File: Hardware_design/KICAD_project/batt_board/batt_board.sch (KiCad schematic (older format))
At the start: 52 parts, among them J11 battery_plug_in, J2 Conn_01x02, J3 Conn_01x02, J4 Conn_01x02, J5 Conn_01x02, U1 TPS5430DDA, U2 AMS1117-3.3

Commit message: batt board: refine the name of sockets
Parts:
- C3: footprint Capacitor_SMD:C_0603_1608Metric_Pad1.08x0.95mm_HandSolder -> Capacitor_Tantalum_SMD:CP_EIA-3528-21_Kemet-B
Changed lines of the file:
@@
 	8100 2700 8700 2700
-Wire Wire Line
-	8200 2800 8200 3050
 Wire Wire Line
 	8200 2800 8700 2800
@@
 $EndComp
 $Comp
-L Device:R_Small_US R11
-U 1 1 60410FC3
-P 8300 3150
-F 0 "R11" H 8368 3196 50  0000 L CNN
-F 1 "22" H 8368 3105 50  0000 L CNN
-F 2 "Resistor_SMD:R_0603_1608Metric_Pad0.98x0.95mm_HandSolder" H 8300 3150 50  0001 C CNN
-F 3 "~" H 8300 3150 50  0001 C CNN
-	1    8300 3150
-	1    0    0    -1
-$EndComp
-$Comp
-L Device:R_Small_US R12
-U 1 1 604142BD
-P 8400 3150
-F 0 "R12" H 8468 3196 50  0000 L CNN
-F 1 "22" H 8468 3105 50  0000 L CNN
-F 2 "Resistor_SMD:R_0603_1608Metric_Pad0.98x0.95mm_HandSolder" H 8400 3150 50  0001 C CNN
-F 3 "~" H 8400 3150 50  0001 C CNN
-	1    8400 3150
-	1    0    0    -1
-$EndComp
-$Comp
 L Device:R_Small_US R13
 U 1 1 60417C9B
@@
 	8200 3250 8200 3350
 Wire Wire Line
-	8300 3050 8300 2900
-Wire Wire Line
 	8400 3250 8400 3350
 Wire Wire Line
@@
 F 0 "C3" H 3191 2146 50  0000 L CNN
 F 1 "220uF" H 3191 2055 50  0000 L CNN
-F 2 "Capacitor_SMD:C_0603_1608Metric_Pad1.08x0.95mm_HandSolder" H 3100 2100 50  0001 C CNN
+F 2 "Capacitor_Tantalum_SMD:CP_EIA-3528-21_Kemet-B" H 3100 2100 50  0001 C CNN
 F 3 "~" H 3100 2100 50  0001 C CNN
 	1    3100 2100
@@
 	1650 2150 950  2150
 Connection ~ 1650 2150
+Wire Wire Line
+	8300 3050 8300 2900
+Wire Wire Line
+	8200 2800 8200 3050
+$Comp
+L Device:R_Small_US R11
+U 1 1 60410FC3
+P 8300 3150
+F 0 "R11" H 8368 3196 50  0000 L CNN
+F 1 "22" H 8368 3105 50  0000 L CNN
+F 2 "Resistor_SMD:R_0603_1608Metric_Pad0.98x0.95mm_HandSolder" H 8300 3150 50  0001 C CNN
+F 3 "~" H 8300 3150 50  0001 C CNN
+	1    8300 3150
+	1    0    0    -1
+$EndComp
+$Comp
+L Device:R_Small_US R12
+U 1 1 604142BD
+P 8400 3150
+F 0 "R12" H 8468 3196 50  0000 L CNN
+F 1 "22" H 8468 3105 50  0000 L CNN
+F 2 "Resistor_SMD:R_0603_1608Metric_Pad0.98x0.95mm_HandSolder" H 8400 3150 50  0001 C CNN
+F 3 "~" H 8400 3150 50  0001 C CNN
+	1    8400 3150
+	1    0    0    -1
+$EndComp
 $EndSCHEMATC

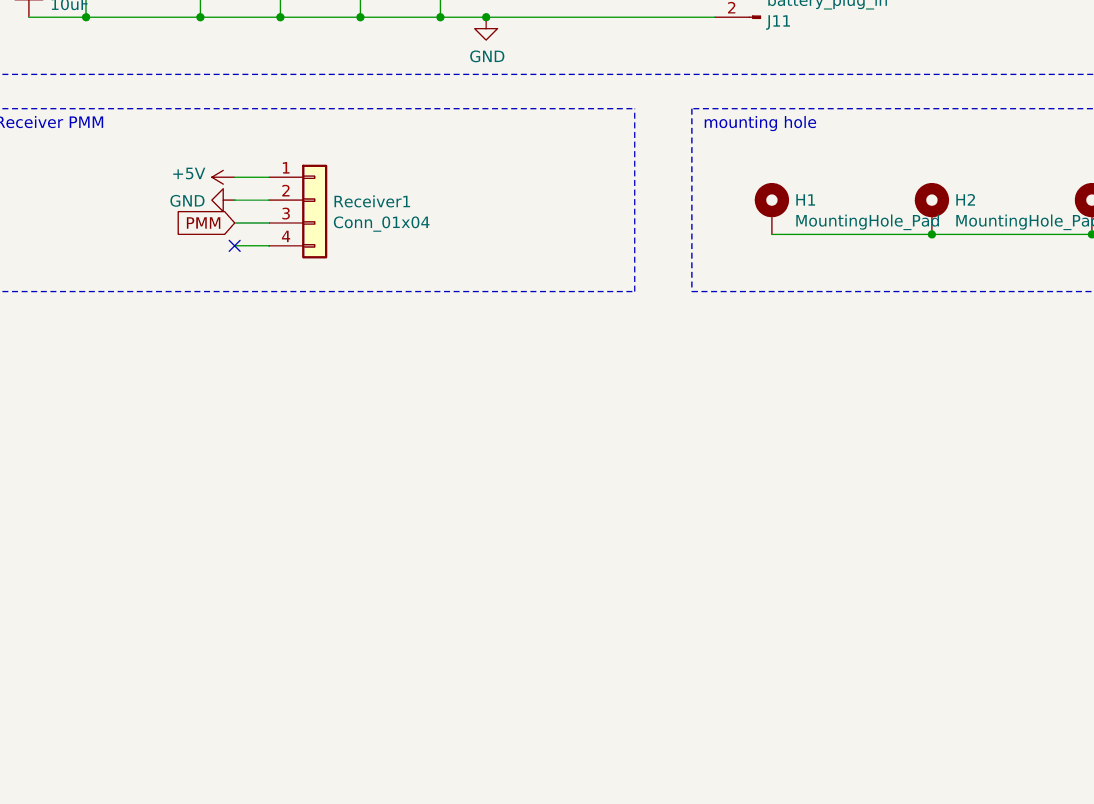
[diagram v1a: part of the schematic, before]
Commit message: 完善了供电板，增加了 IMU的外围传感电路设计
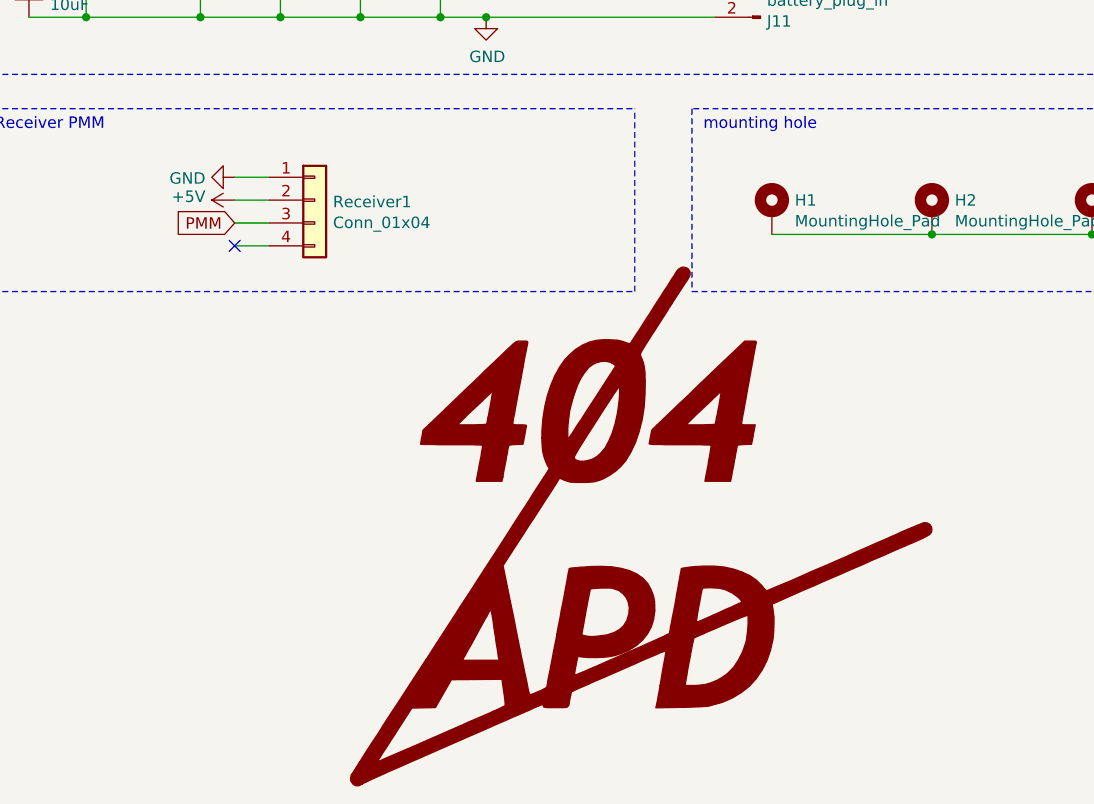
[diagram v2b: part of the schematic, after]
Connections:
- net +5V: now also Receiver1.2 (Pin_2); no longer Receiver1.1 (Pin_1)
- net GND: now also Receiver1.1 (Pin_1); no longer Receiver1.2 (Pin_2)
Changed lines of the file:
@@
 L power:GND #PWR0105
 U 1 1 602F3780
-P 1600 5100
-F 0 "#PWR0105" H 1600 4850 50  0001 C CNN
-F 1 "GND" V 1605 4972 50  0000 R CNN
-F 2 "" H 1600 5100 50  0001 C CNN
-F 3 "" H 1600 5100 50  0001 C CNN
-	1    1600 5100
+P 1600 5000
+F 0 "#PWR0105" H 1600 4750 50  0001 C CNN
+F 1 "GND" V 1605 4872 50  0000 R CNN
+F 2 "" H 1600 5000 50  0001 C CNN
+F 3 "" H 1600 5000 50  0001 C CNN
+	1    1600 5000
 	0    1    1    0
 $EndComp
@@
 L power:+5V #PWR0103
 U 1 1 604C3AB9
-P 1600 5000
-F 0 "#PWR0103" H 1600 4850 50  0001 C CNN
-F 1 "+5V" V 1615 5128 50  0000 L CNN
-F 2 "" H 1600 5000 50  0001 C CNN
-F 3 "" H 1600 5000 50  0001 C CNN
-	1    1600 5000
+P 1600 5100
+F 0 "#PWR0103" H 1600 4950 50  0001 C CNN
+F 1 "+5V" V 1615 5228 50  0000 L CNN
+F 2 "" H 1600 5100 50  0001 C CNN
+F 3 "" H 1600 5100 50  0001 C CNN
+	1    1600 5100
 	0    -1   -1   0
 $EndComp
@@
 	1    0    0    -1
 $EndComp
+$Comp
+L 404APD:LOGO #G1
+U 1 1 603449C8
+P 3350 6550
+F 0 "#G1" H 3350 5217 60  0001 C CNN
+F 1 "LOGO" H 3350 7883 60  0001 C CNN
+F 2 "" H 3350 6550 50  0001 C CNN
+F 3 "" H 3350 6550 50  0001 C CNN
+	1    3350 6550
+	1    0    0    -1
+$EndComp

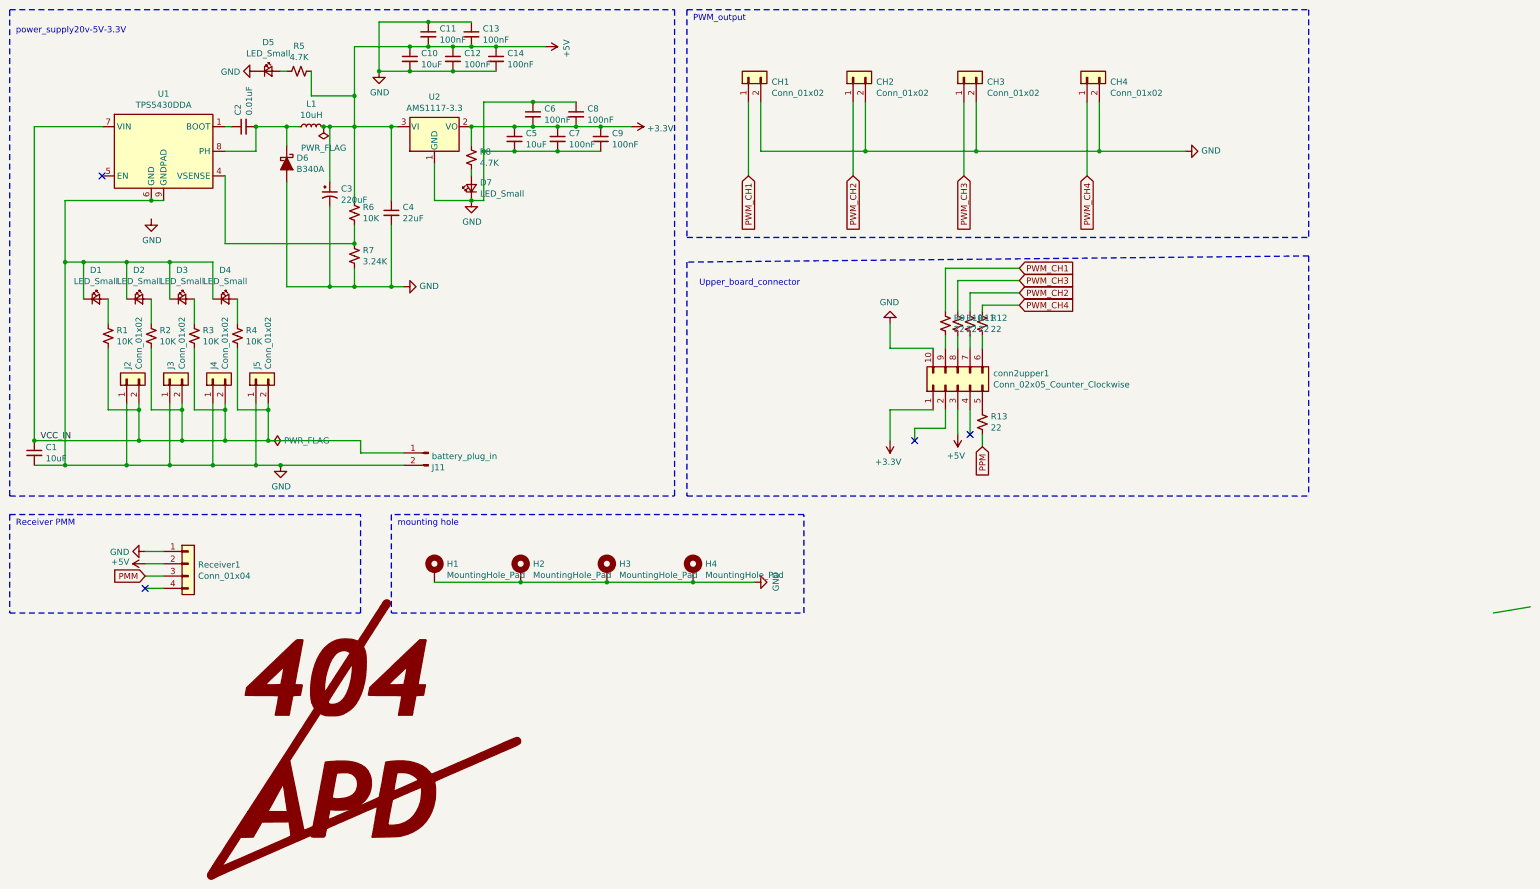
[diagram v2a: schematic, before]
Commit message: 控制系统硬件设计完成，电源板正式发布v1.0.0 控制板打样v0.2.0测试
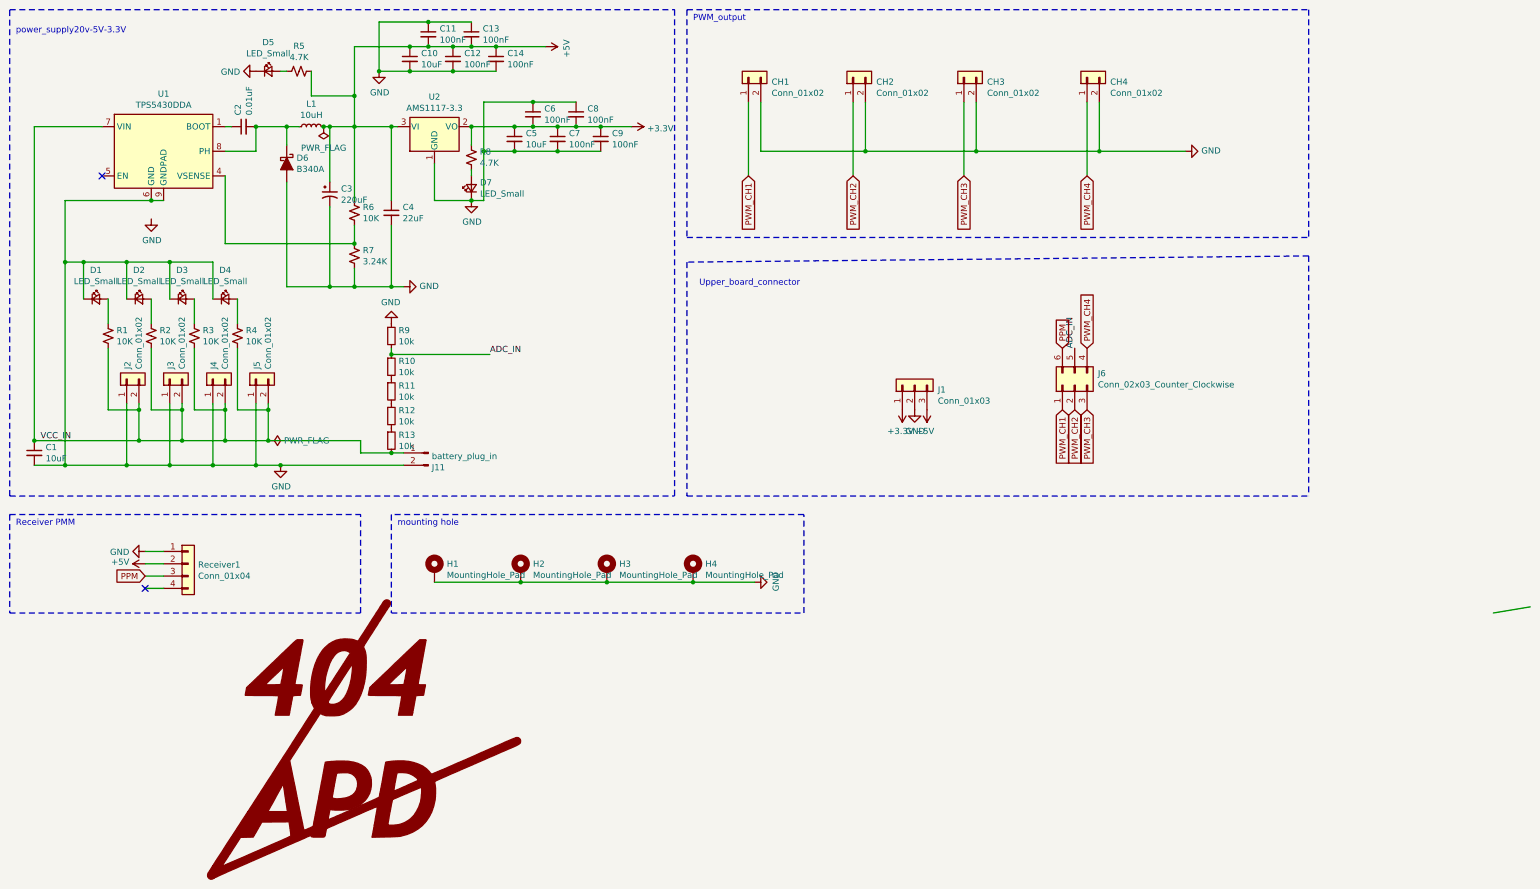
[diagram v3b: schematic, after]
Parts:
- removed R10, R11, R12, R13, R9: 22, Resistor_SMD:R_0603_1608Metric_Pad0.98x0.95mm_HandSolder, symbol Device:R_Small_US
- removed conn2upper1: Conn_02x05_Counter_Clockwise, Connector_PinSocket_2.54mm:PinSocket_2x05_P2.54mm_Horizontal, symbol Connector_Generic:Conn_02x05_Counter_Clockwise
- added J1: Conn_01x03, Connector_PinSocket_2.54mm:PinSocket_1x03_P2.54mm_Vertical, symbol Connector_Generic:Conn_01x03
- added J6: Conn_02x03_Counter_Clockwise, Connector_PinSocket_1.27mm:PinSocket_2x03_P1.27mm_Vertical_SMD, symbol Connector_Generic:Conn_02x03_Counter_Clockwise
- added R10, R11, R12, R13, R9: 10k, Resistor_SMD:R_0603_1608Metric_Pad0.98x0.95mm_HandSolder, symbol Device:R_Small
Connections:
- net PMM is gone; now on net PPM: Receiver1.3 (Pin_3)
- net +3V3: now also J1.1 (Pin_1)
- net +5V: now also J1.3 (Pin_3)
- net GND: now also J1.2 (Pin_2), R9.1
- net PPM: now also J6.6 (Pin_6)
- net PWM_CH1: now also J6.1 (Pin_1)
- net PWM_CH2: now also J6.2 (Pin_2)
- net PWM_CH3: now also J6.3 (Pin_3)
- net PWM_CH4: now also J6.4 (Pin_4)
- net VCC_IN: now also R13.2
- new net: R12.2, R13.1
- new net: R11.2, R12.1
- new net: R10.2, R11.1
- new net ADC_IN: J6.5 (Pin_5), R10.1, R9.2
- no-connect marks 4 -> 2
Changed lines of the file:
@@
 Sheet 1 1
 Title "power_suplly"
-Date "2021-02-14"
-Rev "0.1"
+Date "2021-03-01"
+Rev "0.2"
 Comp ""
 Comment1 ""
@@
 	1600 5100 1750 5100
 Text GLabel 1600 5200 0    50   Input ~ 0
-PMM
+PPM
 Wire Wire Line
 	1750 5300 1600 5300
@@
 Upper_board_connector\n
 $Comp
-L Connector_Generic:Conn_02x05_Counter_Clockwise conn2upper1
-U 1 1 603BA7D0
-P 8200 3650
-F 0 "conn2upper1" V 8296 3362 50  0000 R CNN
-F 1 "Conn_02x05_Counter_Clockwise" V 8205 3362 50  0000 R CNN
-F 2 "Connector_PinSocket_2.54mm:PinSocket_2x05_P2.54mm_Horizontal" H 8200 3650 50  0001 C CNN
-F 3 "~" H 8200 3650 50  0001 C CNN
-	1    8200 3650
-	0    -1   -1   0
-$EndComp
-Wire Wire Line
-	8000 3350 7650 3350
-Wire Wire Line
-	8000 3850 7650 3850
-Wire Wire Line
-	7650 3850 7650 4100
-$Comp
 L power:GND #PWR0109
 U 1 1 603C3758
-P 7650 3150
-F 0 "#PWR0109" H 7650 2900 50  0001 C CNN
-F 1 "GND" H 7655 2977 50  0000 C CNN
-F 2 "" H 7650 3150 50  0001 C CNN
-F 3 "" H 7650 3150 50  0001 C CNN
-	1    7650 3150
-	-1   0    0    1
-$EndComp
-Wire Wire Line
-	8200 3850 8200 4050
-Wire Wire Line
-	8300 3850 8300 4050
-Text GLabel 8700 2700 2    50   Input ~ 0
+P 7850 3850
+F 0 "#PWR0109" H 7850 3600 50  0001 C CNN
+F 1 "GND" H 7855 3677 50  0000 C CNN
+F 2 "" H 7850 3850 50  0001 C CNN
+F 3 "" H 7850 3850 50  0001 C CNN
+	1    7850 3850
+	1    0    0    -1
+$EndComp
+Text GLabel 9050 3850 3    50   Input ~ 0
 PWM_CH1
-Text GLabel 8700 2800 2    50   Input ~ 0
+Text GLabel 9250 3850 3    50   Input ~ 0
 PWM_CH3
-Text GLabel 8700 2900 2    50   Input ~ 0
+Text GLabel 9150 3850 3    50   Input ~ 0
 PWM_CH2
-Text GLabel 8700 3000 2    50   Input ~ 0
+Text GLabel 9250 3350 1    50   Input ~ 0
 PWM_CH4
-Text GLabel 8400 4150 3    50   Input ~ 0
+Text GLabel 9050 3350 1    50   Input ~ 0
 PPM
-NoConn ~ 8300 4050
-Wire Wire Line
-	8100 3350 8100 3250
-Wire Wire Line
-	8100 2700 8700 2700
-Wire Wire Line
-	8200 2800 8700 2800
-Wire Wire Line
-	8300 3350 8300 3250
-Wire Wire Line
-	8300 2900 8700 2900
-Wire Wire Line
-	8400 3000 8400 3050
-Wire Wire Line
-	8400 3000 8700 3000
-$Comp
-L Device:R_Small_US R9
-U 1 1 60408BAB
-P 8100 3150
-F 0 "R9" H 8168 3196 50  0000 L CNN
-F 1 "22" H 8168 3105 50  0000 L CNN
-F 2 "Resistor_SMD:R_0603_1608Metric_Pad0.98x0.95mm_HandSolder" H 8100 3150 50  0001 C CNN
-F 3 "~" H 8100 3150 50  0001 C CNN
-	1    8100 3150
-	1    0    0    -1
-$EndComp
-Wire Wire Line
-	8100 3050 8100 2700
-$Comp
-L Device:R_Small_US R10
-U 1 1 6040DAE6
-P 8200 3150
-F 0 "R10" H 8268 3196 50  0000 L CNN
-F 1 "22" H 8268 3105 50  0000 L CNN
-F 2 "Resistor_SMD:R_0603_1608Metric_Pad0.98x0.95mm_HandSolder" H 8200 3150 50  0001 C CNN
-F 3 "~" H 8200 3150 50  0001 C CNN
-	1    8200 3150
-	1    0    0    -1
-$EndComp
-$Comp
-L Device:R_Small_US R13
-U 1 1 60417C9B
-P 8400 3950
-F 0 "R13" H 8468 3996 50  0000 L CNN
-F 1 "22" H 8468 3905 50  0000 L CNN
-F 2 "Resistor_SMD:R_0603_1608Metric_Pad0.98x0.95mm_HandSolder" H 8400 3950 50  0001 C CNN
-F 3 "~" H 8400 3950 50  0001 C CNN
-	1    8400 3950
-	1    0    0    -1
-$EndComp
 $Comp
 L power:GND #PWR0111
@@
 	3100 2200 3100 2850
 Wire Wire Line
-	8200 3250 8200 3350
-Wire Wire Line
-	8400 3250 8400 3350
-Wire Wire Line
 	2500 1550 2750 1550
 Wire Wire Line
@@
 Wire Wire Line
 	3100 1550 3300 1550
-Wire Wire Line
-	8400 4050 8400 4150
 $Comp
 L power:+3.3V #PWR0110
 U 1 1 603C41F2
-P 7650 4100
-F 0 "#PWR0110" H 7650 3950 50  0001 C CNN
-F 1 "+3.3V" H 7665 4273 50  0000 C CNN
-F 2 "" H 7650 4100 50  0001 C CNN
-F 3 "" H 7650 4100 50  0001 C CNN
-	1    7650 4100
+P 7750 3850
+F 0 "#PWR0110" H 7750 3700 50  0001 C CNN
+F 1 "+3.3V" H 7765 4023 50  0000 C CNN
+F 2 "" H 7750 3850 50  0001 C CNN
+F 3 "" H 7750 3850 50  0001 C CNN
+	1    7750 3850
 	-1   0    0    1
 $EndComp
@@
 Wire Wire Line
 	5350 5250 6050 5250
-Wire Wire Line
-	6050 5250 6550 5250
 Connection ~ 6050 5250
-$Comp
-L power:GND #PWR0104
-U 1 1 60310458
-P 6550 5250
-F 0 "#PWR0104" H 6550 5000 50  0001 C CNN
-F 1 "GND" H 6555 5077 50  0000 C CNN
-F 2 "" H 6550 5250 50  0001 C CNN
-F 3 "" H 6550 5250 50  0001 C CNN
-	1    6550 5250
-	0    -1   -1   0
-$EndComp
 Connection ~ 950  4300
 Wire Wire Line
@@
 	3350 4100 3350 4200
 Wire Wire Line
-	3350 4200 3700 4200
+	3350 4200 3600 4200
 Wire Wire Line
 	1300 3850 1550 3850
@@
 Wire Wire Line
 	1750 5000 1600 5000
-Wire Wire Line
-	8100 3850 8100 4000
-Wire Wire Line
-	8100 4000 7850 4000
-Wire Wire Line
-	7850 4000 7850 4100
-Wire Wire Line
-	7650 3150 7650 3350
 $Comp
 L power:+5V #PWR0113
 U 1 1 6084A891
-P 8200 4050
-F 0 "#PWR0113" H 8200 3900 50  0001 C CNN
-F 1 "+5V" H 8215 4223 50  0000 C CNN
-F 2 "" H 8200 4050 50  0001 C CNN
-F 3 "" H 8200 4050 50  0001 C CNN
-	1    8200 4050
+P 7950 3850
+F 0 "#PWR0113" H 7950 3700 50  0001 C CNN
+F 1 "+5V" H 7965 4023 50  0000 C CNN
+F 2 "" H 7950 3850 50  0001 C CNN
+F 3 "" H 7950 3850 50  0001 C CNN
+	1    7950 3850
 	-1   0    0    1
 $EndComp
-NoConn ~ 7850 4100
 $Comp
 L Device:C_Small C4
@@
 	1650 2150 950  2150
 Connection ~ 1650 2150
-Wire Wire Line
-	8300 3050 8300 2900
-Wire Wire Line
-	8200 2800 8200 3050
-$Comp
-L Device:R_Small_US R11
-U 1 1 60410FC3
-P 8300 3150
-F 0 "R11" H 8368 3196 50  0000 L CNN
-F 1 "22" H 8368 3105 50  0000 L CNN
-F 2 "Resistor_SMD:R_0603_1608Metric_Pad0.98x0.95mm_HandSolder" H 8300 3150 50  0001 C CNN
-F 3 "~" H 8300 3150 50  0001 C CNN
-	1    8300 3150
-	1    0    0    -1
-$EndComp
-$Comp
-L Device:R_Small_US R12
-U 1 1 604142BD
-P 8400 3150
-F 0 "R12" H 8468 3196 50  0000 L CNN
-F 1 "22" H 8468 3105 50  0000 L CNN
-F 2 "Resistor_SMD:R_0603_1608Metric_Pad0.98x0.95mm_HandSolder" H 8400 3150 50  0001 C CNN
-F 3 "~" H 8400 3150 50  0001 C CNN
-	1    8400 3150
-	1    0    0    -1
-$EndComp
 $Comp
 L 404APD:LOGO #G1
@@
 	1    0    0    -1
 $EndComp
+$Comp
+L Device:R_Small R13
+U 1 1 6059E8B9
+P 3600 4100
+F 0 "R13" H 3659 4146 50  0000 L CNN
+F 1 "10k" H 3659 4055 50  0000 L CNN
+F 2 "Resistor_SMD:R_0603_1608Metric_Pad0.98x0.95mm_HandSolder" H 3600 4100 50  0001 C CNN
+F 3 "~" H 3600 4100 50  0001 C CNN
+	1    3600 4100
+	1    0    0    -1
+$EndComp
+$Comp
+L Device:R_Small R12
+U 1 1 605A041B
+P 3600 3900
+F 0 "R12" H 3659 3946 50  0000 L CNN
+F 1 "10k" H 3659 3855 50  0000 L CNN
+F 2 "Resistor_SMD:R_0603_1608Metric_Pad0.98x0.95mm_HandSolder" H 3600 3900 50  0001 C CNN
+F 3 "~" H 3600 3900 50  0001 C CNN
+	1    3600 3900
+	1    0    0    -1
+$EndComp
+$Comp
+L Device:R_Small R10
+U 1 1 605AC6B4
+P 3600 3500
+F 0 "R10" H 3659 3546 50  0000 L CNN
+F 1 "10k" H 3659 3455 50  0000 L CNN
+F 2 "Resistor_SMD:R_0603_1608Metric_Pad0.98x0.95mm_HandSolder" H 3600 3500 50  0001 C CNN
+F 3 "~" H 3600 3500 50  0001 C CNN
+	1    3600 3500
+	1    0    0    -1
+$EndComp
+$Comp
+L Device:R_Small R9
+U 1 1 605B2AEA
+P 3600 3250
+F 0 "R9" H 3659 3296 50  0000 L CNN
+F 1 "10k" H 3659 3205 50  0000 L CNN
+F 2 "Resistor_SMD:R_0603_1608Metric_Pad0.98x0.95mm_HandSolder" H 3600 3250 50  0001 C CNN
+F 3 "~" H 3600 3250 50  0001 C CNN
+	1    3600 3250
+	1    0    0    -1
+$EndComp
+Connection ~ 3600 4200
+Wire Wire Line
+	3600 4200 3700 4200
+$Comp
+L Device:R_Small R11
+U 1 1 605A64DF
+P 3600 3700
+F 0 "R11" H 3659 3746 50  0000 L CNN
+F 1 "10k" H 3659 3655 50  0000 L CNN
+F 2 "Resistor_SMD:R_0603_1608Metric_Pad0.98x0.95mm_HandSolder" H 3600 3700 50  0001 C CNN
+F 3 "~" H 3600 3700 50  0001 C CNN
+	1    3600 3700
+	1    0    0    -1
+$EndComp
+Wire Wire Line
+	3600 3350 3600 3400
+Wire Wire Line
+	3600 3400 4400 3400
+Connection ~ 3600 3400
+Text Label 4400 3400 0    50   ~ 0
+ADC_IN
+$Comp
+L power:GND #PWR01
+U 1 1 60616D77
+P 3600 3150
+F 0 "#PWR01" H 3600 2900 50  0001 C CNN
+F 1 "GND" H 3605 2977 50  0000 C CNN
+F 2 "" H 3600 3150 50  0001 C CNN
+F 3 "" H 3600 3150 50  0001 C CNN
+	1    3600 3150
+	-1   0    0    1
+$EndComp
+$Comp
+L Connector_Generic:Conn_02x03_Counter_Clockwise J6
+U 1 1 6063B7D7
+P 9150 3650
+F 0 "J6" V 9246 3462 50  0000 R CNN
+F 1 "Conn_02x03_Counter_Clockwise" V 9155 3462 50  0000 R CNN
+F 2 "Connector_PinSocket_1.27mm:PinSocket_2x03_P1.27mm_Vertical_SMD" H 9150 3650 50  0001 C CNN
+F 3 "~" H 9150 3650 50  0001 C CNN
+	1    9150 3650
+	0    -1   -1   0
+$EndComp
+$Comp
+L Connector_Generic:Conn_01x03 J1
+U 1 1 60693E51
+P 7850 3650
+F 0 "J1" V 7814 3462 50  0000 R CNN
+F 1 "Conn_01x03" V 7723 3462 50  0000 R CNN
+F 2 "Connector_PinSocket_2.54mm:PinSocket_1x03_P2.54mm_Vertical" H 7850 3650 50  0001 C CNN
+F 3 "~" H 7850 3650 50  0001 C CNN
+	1    7850 3650
+	0    -1   -1   0
+$EndComp
+Text Label 9150 3350 1    50   ~ 0
+ADC_IN
+Wire Wire Line
+	6050 5250 6550 5250
+$Comp
+L power:GND #PWR0104
+U 1 1 60310458
+P 6550 5250
+F 0 "#PWR0104" H 6550 5000 50  0001 C CNN
+F 1 "GND" H 6555 5077 50  0000 C CNN
+F 2 "" H 6550 5250 50  0001 C CNN
+F 3 "" H 6550 5250 50  0001 C CNN
+	1    6550 5250
+	0    -1   -1   0
+$EndComp
 $EndSCHEMATC
